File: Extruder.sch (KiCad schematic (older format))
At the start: 2 parts, among them J10 Probe, J11 Extruder Heater

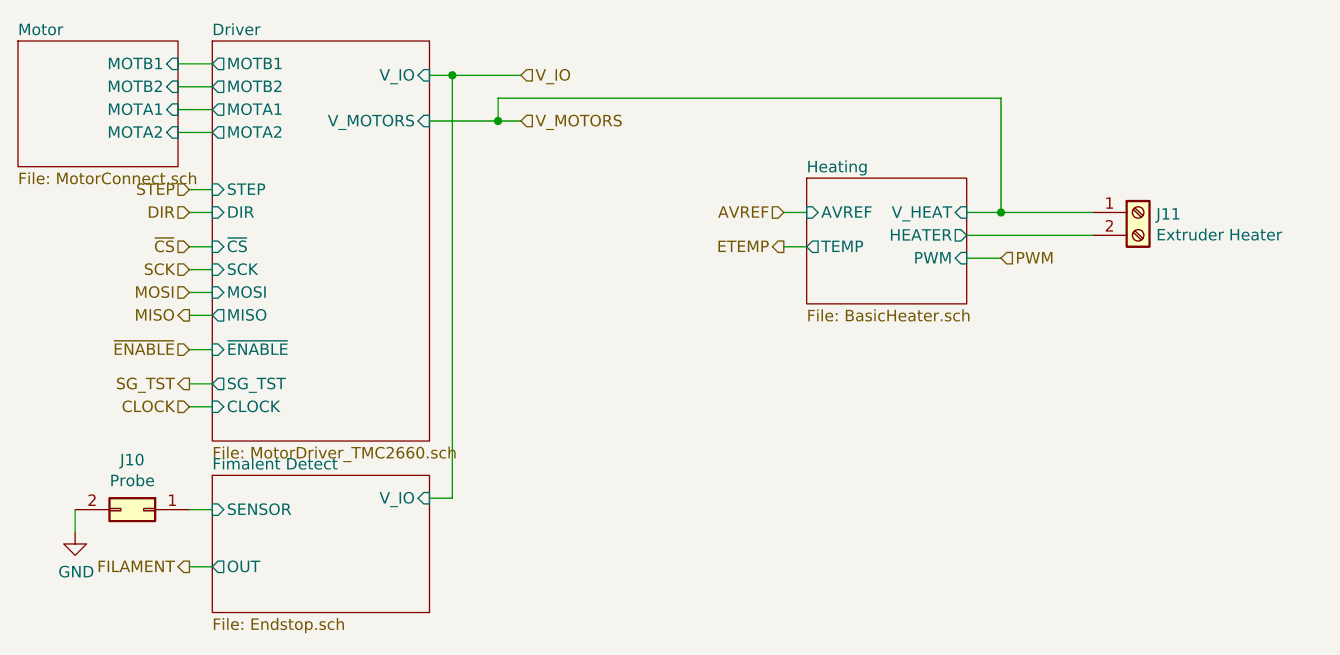
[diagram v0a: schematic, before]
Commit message: Rename some somponents to suite PNP process.
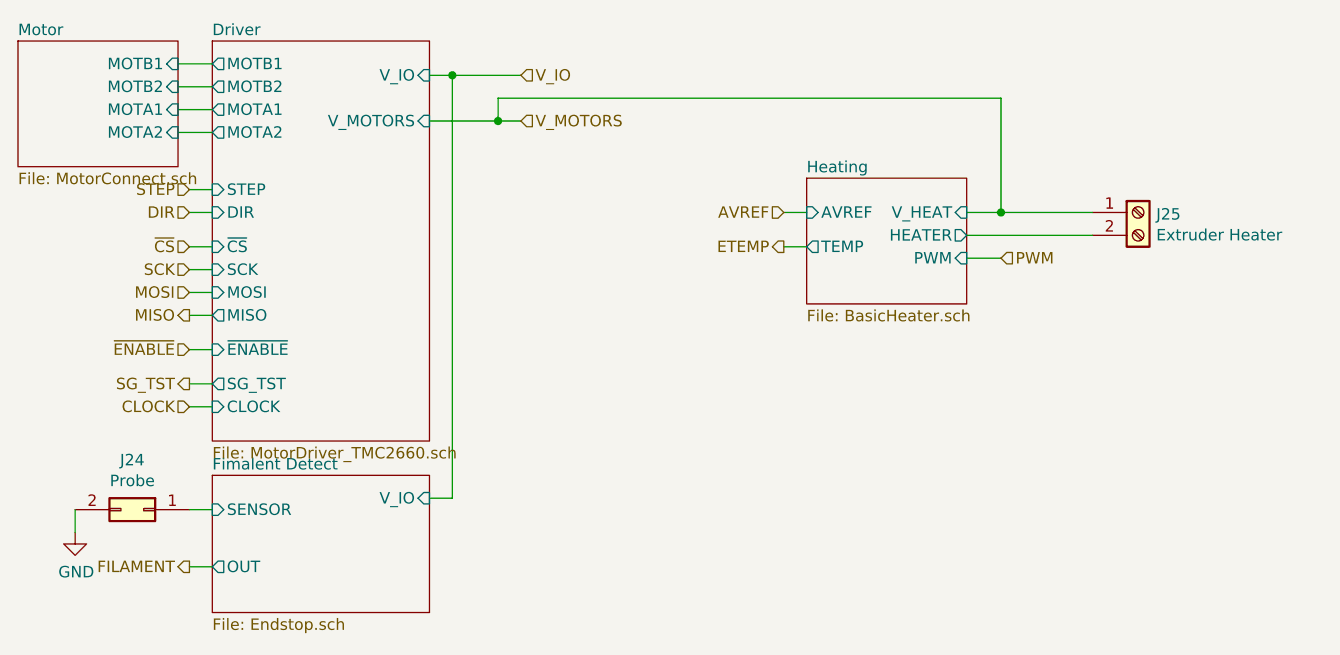
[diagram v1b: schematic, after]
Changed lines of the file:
@@
 $Descr A4 11693 8268
 encoding utf-8
-Sheet 3 35
+Sheet 25 35
 Title ""
 Date ""
@@
 AR Path="/5AC337B6/5ACBE919/5AD4BF35" Ref="J10"  Part="1"
 AR Path="/5AC337B6/5AD9F95A/5AD4BF35" Ref="J24"  Part="1"
-F 0 "J10" H 2450 4217 50  0000 C CNN
+F 0 "J24" H 2450 4217 50  0000 C CNN
 F 1 "Probe" H 2450 4126 50  0000 C CNN
 F 2 "Connector_PinHeader_2.54mm:PinHeader_1x02_P2.54mm_Vertical" H 2400 4000 50  0001 C CNN
@@
 AR Path="/5AC337B6/5ACBE919/5AD53BDD" Ref="J11"  Part="1"
 AR Path="/5AC337B6/5AD9F95A/5AD53BDD" Ref="J25"  Part="1"
-F 0 "J11" H 6829 2692 50  0000 L CNN
+F 0 "J25" H 6829 2692 50  0000 L CNN
 F 1 "Extruder Heater" H 6829 2601 50  0000 L CNN
 F 2 "PrntrBoardV1:TerminalBlock_Phoenix_PT-1,5-2-3.5-H_1x02_P3.50mm_Horizontal" H 6750 2700 50  0001 C CNN
